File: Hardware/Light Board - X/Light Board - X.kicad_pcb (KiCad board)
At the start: 2 copper layers, 51.7 x 38.4 mm, 12 parts, among them J1 V+, J2 V-

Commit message: Added production file generation tools
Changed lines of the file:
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@@
 	)
 	(paper "A")
+	(title_block
+		(title "Light Board - X")
+		(date "2025-08-10")
+		(rev "${REV_BOARD}")
+		(comment 1 "Isaac Rex")
+	)
 	(layers
 		(0 "F.Cu" signal)
@@
 		(35 "F.Fab" user)
 		(33 "B.Fab" user)
-		(39 "User.1" user)
-		(41 "User.2" user)
-		(43 "User.3" user)
+		(39 "User.1" user "User.FabDrawing")
+		(41 "User.2" user "User.TopAsyDrawing")
+		(43 "User.3" user "User.BotAsyDrawing")
 		(45 "User.4" user)
 		(47 "User.5" user)
@@
 		)
 		(embedded_fonts no)
-		(model "${KICAD9_3DMODEL_DIR}/LED_SMD.3dshapes/LED_Everlight-SMD3528_3.5x2.8mm_67-21ST.step"
-			(offset
-				(xyz 0 0 0)
-			)
-			(scale
-				(xyz 1 1 1)
-			)
-			(rotate
-				(xyz 0 0 0)
-			)
-		)
 	)
 	(footprint "TestPoint:TestPoint_Pad_2.0x2.0mm"
@@
 		)
 		(embedded_fonts no)
-		(model "${KICAD9_3DMODEL_DIR}/LED_SMD.3dshapes/LED_Everlight-SMD3528_3.5x2.8mm_67-21ST.step"
-			(offset
-				(xyz 0 0 0)
-			)
-			(scale
-				(xyz 1 1 1)
-			)
-			(rotate
-				(xyz 0 0 0)
-			)
-		)
 	)
 	(footprint "LED_SMD:LED_Everlight-SMD3528_3.5x2.8mm_67-21ST"
@@
 		(tags "LED 3528")
 		(property "Reference" "D8"
-			(at -3.91337 -0.024604 320)
+			(at -3.91337 -0.024605 140)
 			(layer "F.SilkS")
 			(effects
@@
 		)
 		(property "Value" "White"
-			(at 0 2.5 320)
+			(at 0 2.5 140)
 			(layer "F.Fab")
 			(effects
@@
 		)
 		(fp_text user "${REFERENCE}"
-			(at 0 0 320)
+			(at 0 0 140)
 			(layer "F.Fab")
 			(effects
@@
 		)
 		(embedded_fonts no)
-		(model "${KICAD9_3DMODEL_DIR}/LED_SMD.3dshapes/LED_Everlight-SMD3528_3.5x2.8mm_67-21ST.step"
-			(offset
-				(xyz 0 0 0)
-			)
-			(scale
-				(xyz 1 1 1)
-			)
-			(rotate
-				(xyz 0 0 0)
-			)
-		)
 	)
 	(footprint "LED_SMD:LED_Everlight-SMD3528_3.5x2.8mm_67-21ST"
@@
 		)
 		(embedded_fonts no)
-		(model "${KICAD9_3DMODEL_DIR}/LED_SMD.3dshapes/LED_Everlight-SMD3528_3.5x2.8mm_67-21ST.step"
-			(offset
-				(xyz 0 0 0)
-			)
-			(scale
-				(xyz 1 1 1)
-			)
-			(rotate
-				(xyz 0 0 0)
-			)
-		)
 	)
 	(footprint "LED_SMD:LED_Everlight-SMD3528_3.5x2.8mm_67-21ST"
@@
 		(tags "LED 3528")
 		(property "Reference" "D6"
-			(at -3.772486 0.012277 220)
+			(at -3.772486 0.012277 40)
 			(layer "F.SilkS")
 			(effects
@@
 		)
 		(property "Value" "White"
-			(at 0 2.5 220)
+			(at 0 2.5 40)
 			(layer "F.Fab")
 			(effects
@@
 		)
 		(fp_text user "${REFERENCE}"
-			(at 0 0 220)
+			(at 0 0 40)
 			(layer "F.Fab")
 			(effects
@@
 		)
 		(embedded_fonts no)
-		(model "${KICAD9_3DMODEL_DIR}/LED_SMD.3dshapes/LED_Everlight-SMD3528_3.5x2.8mm_67-21ST.step"
-			(offset
-				(xyz 0 0 0)
-			)
-			(scale
-				(xyz 1 1 1)
-			)
-			(rotate
-				(xyz 0 0 0)
-			)
-		)
 	)
 	(footprint "LED_SMD:LED_Everlight-SMD3528_3.5x2.8mm_67-21ST"
@@
 		(tags "LED 3528")
 		(property "Reference" "D7"
-			(at -3.84947 -1.268125 220)
+			(at -3.84947 -1.268125 40)
 			(layer "F.SilkS")
 			(effects
@@
 		)
 		(property "Value" "White"
-			(at 0 2.5 220)
+			(at 0 2.5 40)
 			(layer "F.Fab")
 			(effects
@@
 		)
 		(fp_text user "${REFERENCE}"
-			(at 0 0 220)
+			(at 0 0 40)
 			(layer "F.Fab")
 			(effects
@@
 		)
 		(embedded_fonts no)
-		(model "${KICAD9_3DMODEL_DIR}/LED_SMD.3dshapes/LED_Everlight-SMD3528_3.5x2.8mm_67-21ST.step"
-			(offset
-				(xyz 0 0 0)
-			)
-			(scale
-				(xyz 1 1 1)
-			)
-			(rotate
-				(xyz 0 0 0)
-			)
-		)
 	)
 	(footprint "LED_SMD:LED_Everlight-SMD3528_3.5x2.8mm_67-21ST"
@@
 		(tags "LED 3528")
 		(property "Reference" "D9"
-			(at -3.772866 1.203846 320)
+			(at -3.772866 1.203846 140)
 			(layer "F.SilkS")
 			(effects
@@
 		)
 		(property "Value" "White"
-			(at 0 2.5 320)
+			(at 0 2.5 140)
 			(layer "F.Fab")
 			(effects
@@
 		)
 		(fp_text user "${REFERENCE}"
-			(at 0 0 320)
+			(at 0 0 140)
 			(layer "F.Fab")
 			(effects
@@
 		)
 		(embedded_fonts no)
-		(model "${KICAD9_3DMODEL_DIR}/LED_SMD.3dshapes/LED_Everlight-SMD3528_3.5x2.8mm_67-21ST.step"
-			(offset
-				(xyz 0 0 0)
-			)
-			(scale
-				(xyz 1 1 1)
-			)
-			(rotate
-				(xyz 0 0 0)
-			)
-		)
 	)
 	(footprint "TestPoint:TestPoint_Pad_2.0x2.0mm"
@@
 		)
 		(embedded_fonts no)
-		(model "${KICAD9_3DMODEL_DIR}/LED_SMD.3dshapes/LED_Everlight-SMD3528_3.5x2.8mm_67-21ST.step"
-			(offset
-				(xyz 0 0 0)
-			)
-			(scale
-				(xyz 1 1 1)
-			)
-			(rotate
-				(xyz 0 0 0)
-			)
-		)
 	)
 	(footprint "irex_Aesthetic:Logo_irex_2.5x2.8mm_Silk"
@@
 		(tags "LED 3528")
 		(property "Reference" "D2"
-			(at -3.776101 -0.03942 220)
+			(at -3.776101 -0.03942 40)
 			(layer "F.SilkS")
 			(effects
@@
 		)
 		(property "Value" "White"
-			(at 0 2.5 220)
+			(at 0 2.5 40)
 			(layer "F.Fab")
 			(effects
@@
 		)
 		(fp_text user "${REFERENCE}"
-			(at 0 0 220)
+			(at 0 0 40)
 			(layer "F.Fab")
 			(effects
@@
 		)
 		(embedded_fonts no)
-		(model "${KICAD9_3DMODEL_DIR}/LED_SMD.3dshapes/LED_Everlight-SMD3528_3.5x2.8mm_67-21ST.step"
-			(offset
-				(xyz 0 0 0)
-			)
-			(scale
-				(xyz 1 1 1)
-			)
-			(rotate
-				(xyz 0 0 0)
-			)
-		)
 	)
 	(gr_arc
@@
 		)
 		(fill no)
-		(layer "User.1")
+		(layer "User.4")
 	)
 	(gr_circle
@@
 		)
 		(fill no)
-		(layer "User.1")
+		(layer "User.4")
 	)
 	(gr_circle
@@
 		)
 		(fill no)
-		(layer "User.1")
+		(layer "User.4")
 	)
 	(gr_circle
@@
 		)
 		(fill no)
-		(layer "User.1")
+		(layer "User.4")
 	)
 	(gr_circle
@@
 		)
 		(fill no)
-		(layer "User.1")
+		(layer "User.4")
 	)
 	(gr_line
@@
 			(type dash)
 		)
-		(layer "User.1")
+		(layer "User.4")
 	)
 	(gr_line
@@
 			(type dash)
 		)
-		(layer "User.1")
+		(layer "User.4")
 	)
 	(gr_circle
@@
 		)
 		(fill no)
-		(layer "User.1")
+		(layer "User.4")
 	)
 	(gr_circle
@@
 		)
 		(fill no)
-		(layer "User.1")
+		(layer "User.4")
 	)
 	(gr_circle
@@
 		)
 		(fill no)
-		(layer "User.1")
+		(layer "User.4")
 	)
 	(gr_circle
@@
 		)
 		(fill no)
-		(layer "User.1")
+		(layer "User.4")
 	)
 	(gr_text "Light\nBoard X"
@@
 			)
 		)
+	)
+	(dimension
+		(type orthogonal)
+		(layer "User.1")
+		(pts
+			(xy 171.28 90.03) (xy 125.52 89.567813)
+		)
+		(height -6.31)
+		(orientation 0)
+		(format
+			(prefix "")
+			(suffix "")
+			(units 3)
+			(units_format 1)
+			(precision 2)
+		)
+		(style
+			(thickness 0.15)
+			(arrow_length 1.27)
+			(text_position_mode 0)
+			(arrow_direction outward)
+			(extension_height 0.58642)
+			(extension_offset 0.5)
+			(keep_text_aligned yes)
+		)
+		(gr_text "45.76 mm"
+			(at 148.4 82.57 0)
+			(layer "User.1")
+			(effects
+				(font
+					(size 1 1)
+					(thickness 0.15)
+				)
+			)
+		)
+	)
+	(dimension
+		(type orthogonal)
+		(layer "User.1")
+		(pts
+			(xy 122.549919 127.2) (xy 174.250081 127.2)
+		)
+		(height 7.8)
+		(orientation 0)
+		(format
+			(prefix "")
+			(suffix "")
+			(units 3)
+			(units_format 1)
+			(precision 2)
+		)
+		(style
+			(thickness 0.15)
+			(arrow_length 1.27)
+			(text_position_mode 0)
+			(arrow_direction outward)
+			(extension_height 0.58642)
+			(extension_offset 0.5)
+			(keep_text_aligned yes)
+		)
+		(gr_text "51.70 mm"
+			(at 148.4 133.85 0)
+			(layer "User.1")
+			(effects
+				(font
+					(size 1 1)
+					(thickness 0.15)
+				)
+			)
+		)
+	)
+	(dimension
+		(type orthogonal)
+		(layer "User.1")
+		(pts
+			(xy 173.650081 127.79998) (xy 170.679441 89.431346)
+		)
+		(height 8.849919)
+		(orientation 1)
+		(format
+			(prefix "")
+			(suffix "")
+			(units 3)
+			(units_format 1)
+			(precision 2)
+		)
+		(style
+			(thickness 0.15)
+			(arrow_length 1.27)
+			(text_position_mode 0)
+			(arrow_direction outward)
+			(extension_height 0.58642)
+			(extension_offset 0.5)
+			(keep_text_aligned yes)
+		)
+		(gr_text "38.37 mm"
+			(at 181.35 108.615663 90)
+			(layer "User.1")
+			(effects
+				(font
+					(size 1 1)
+					(thickness 0.15)
+				)
+			)
+		)

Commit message: Finished all light boards
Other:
- board text added: "-"
- board text removed: "–"
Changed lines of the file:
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@@
 		)
 	)
-	(gr_text "–"
-		(at 125.3 123.8 0)
+	(gr_text "-"
+		(at 125.6 123.9 0)
 		(layer "F.SilkS")
 		(effects

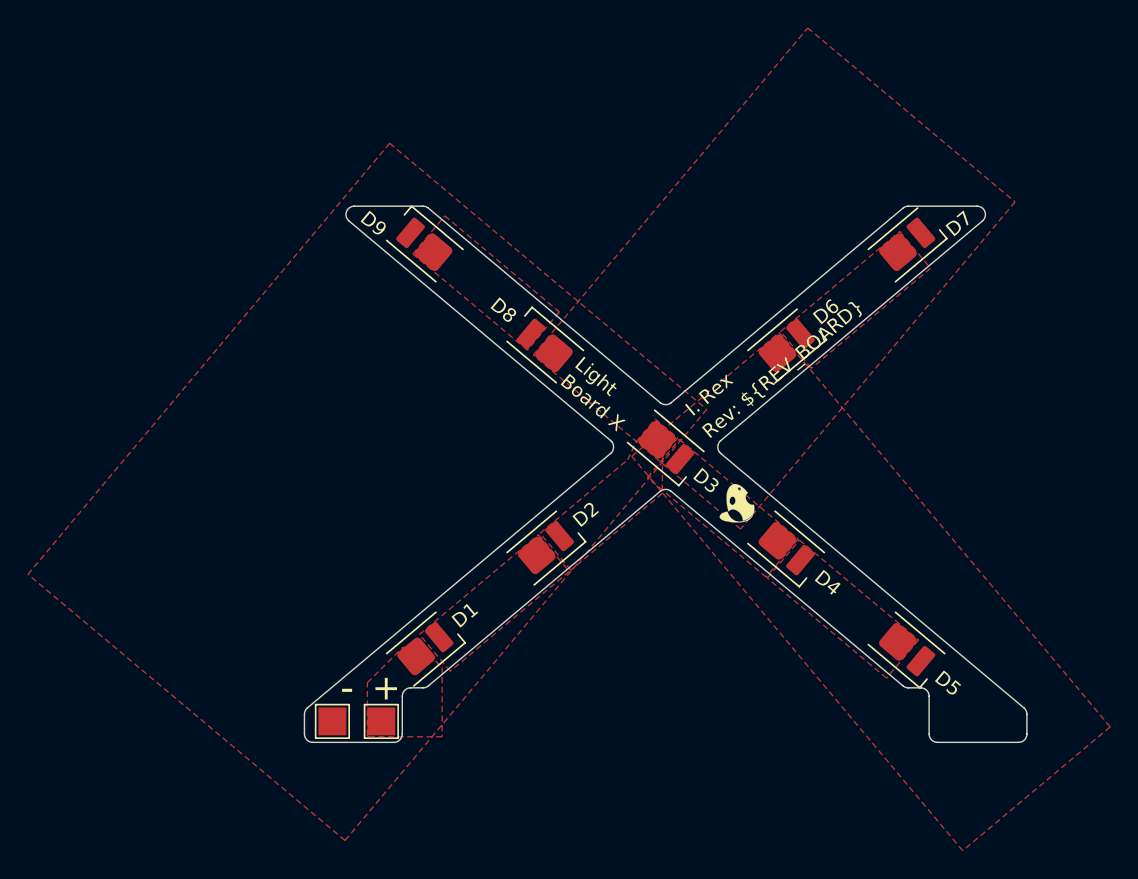
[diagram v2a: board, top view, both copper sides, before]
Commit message: Added LED library and fixed orientation
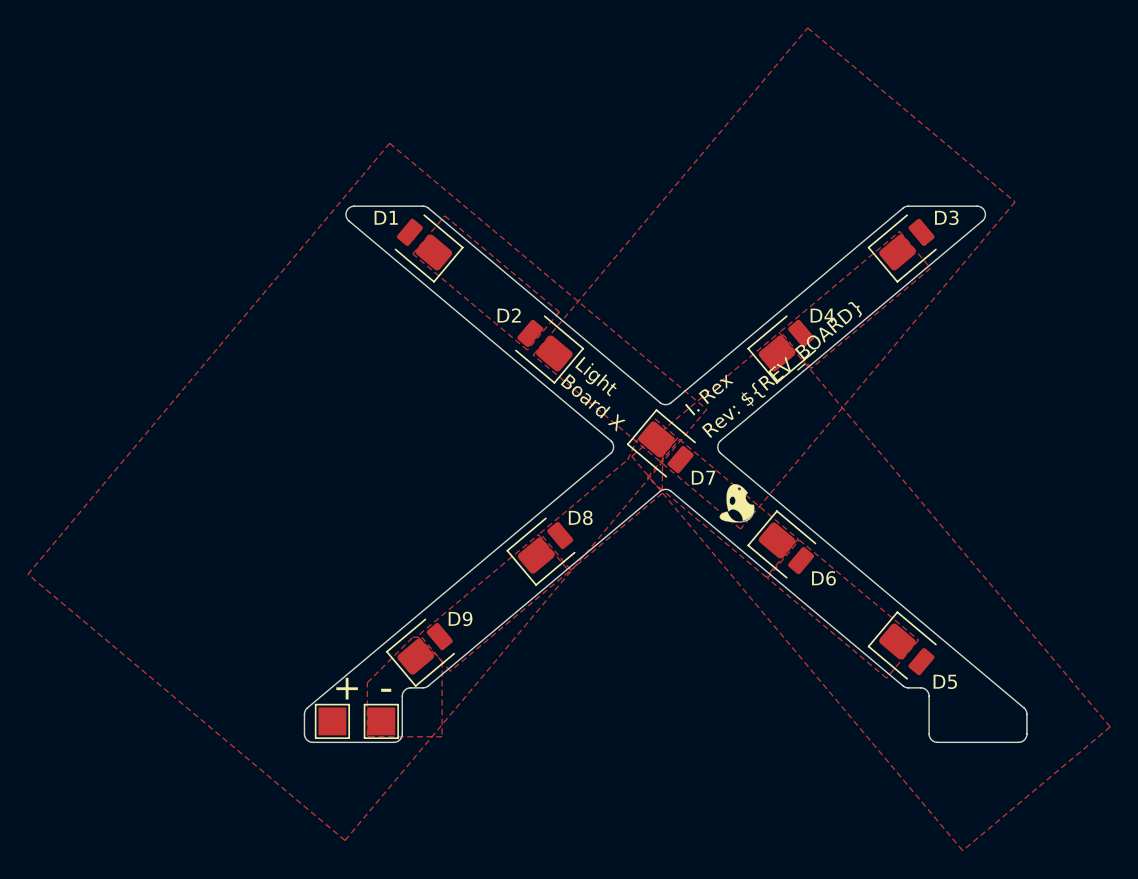
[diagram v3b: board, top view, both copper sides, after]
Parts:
- D1: renamed from D9; footprint LED_SMD:LED_Everlight-SMD3528_3.5x2.8mm_67-21ST -> irex_LED_SMD:LED_Cree_J-Series_SMD2835_2.8x3.5mm
- D2: renamed from D8; footprint LED_SMD:LED_Everlight-SMD3528_3.5x2.8mm_67-21ST -> irex_LED_SMD:LED_Cree_J-Series_SMD2835_2.8x3.5mm
- D3: renamed from D7; footprint LED_SMD:LED_Everlight-SMD3528_3.5x2.8mm_67-21ST -> irex_LED_SMD:LED_Cree_J-Series_SMD2835_2.8x3.5mm
- D4: renamed from D6; footprint LED_SMD:LED_Everlight-SMD3528_3.5x2.8mm_67-21ST -> irex_LED_SMD:LED_Cree_J-Series_SMD2835_2.8x3.5mm
- D5: footprint LED_SMD:LED_Everlight-SMD3528_3.5x2.8mm_67-21ST -> irex_LED_SMD:LED_Cree_J-Series_SMD2835_2.8x3.5mm
- D6: renamed from D4; footprint LED_SMD:LED_Everlight-SMD3528_3.5x2.8mm_67-21ST -> irex_LED_SMD:LED_Cree_J-Series_SMD2835_2.8x3.5mm
- D7: renamed from D3; footprint LED_SMD:LED_Everlight-SMD3528_3.5x2.8mm_67-21ST -> irex_LED_SMD:LED_Cree_J-Series_SMD2835_2.8x3.5mm
- D8: renamed from D2; footprint LED_SMD:LED_Everlight-SMD3528_3.5x2.8mm_67-21ST -> irex_LED_SMD:LED_Cree_J-Series_SMD2835_2.8x3.5mm
- D9: renamed from D1; footprint LED_SMD:LED_Everlight-SMD3528_3.5x2.8mm_67-21ST -> irex_LED_SMD:LED_Cree_J-Series_SMD2835_2.8x3.5mm
- J1: renamed from J2; value V- -> V+
- J2: renamed from J1; value V+ -> V-
- turned D1 to 140 degrees
- turned D2 to 140 degrees
- turned D3 to 40 degrees
- turned D4 to 40 degrees
- turned D5 to -40 degrees
- turned D6 to -40 degrees
- turned D7 to -40 degrees
- turned D8 to 40 degrees
- turned D9 to 40 degrees
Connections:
- D1 pad 1: /V- -> /K_D1
- D1 pad 2: /K_D9 -> /V+
- D2 pad 1: /K_D9 -> /K_D2
- D2 pad 2: /K_D7 -> /K_D1
- D3 pad 1: /K_D7 -> /K_D3
- D3 pad 2: /K_D6 -> /K_D2
- D4 pad 1: /K_D6 -> /K_D4
- D4 pad 2: /K_D5 -> /K_D3
- D6 pad 1: /K_D4 -> /K_D6
- D6 pad 2: /K_D3 -> /K_D5
- D7 pad 1: /K_D3 -> /K_D7
- D7 pad 2: /K_D2 -> /K_D6
- D8 pad 1: /K_D2 -> /K_D8
- D8 pad 2: /K_D1 -> /K_D7
- D9 pad 1: /K_D1 -> /V-
- D9 pad 2: /V+ -> /K_D8
- J1 pad 1: /V- -> /V+
- J2 pad 1: /V+ -> /V-
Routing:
- added copper zone on F.Cu, net /K_D8
- removed copper zone on F.Cu, net /K_D9
